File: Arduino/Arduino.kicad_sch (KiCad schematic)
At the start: 21 parts, among them J1 Conn_01x01, J10 Conn_01x03, J2 Conn_01x01, J3 Digital, J4 Digital, J5 ICSP, J6 Digital, J7 Digital, J8 Barrel_Jack_Switch, J9 Vcc, SW1 Reset, U1 ATmega328P-P, Y1 16MHz

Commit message: Some changes in arduino board.
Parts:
- added C1: 100n, symbol Device:C_Small
- added Q1, Q2: SS8050, Package_TO_SOT_SMD:SOT-23, symbol Transistor_BJT:SS8050
- added R1: 10k, symbol Device:R_Small
- renumbered C1 to C2, C2 to C3, C3 to C4, C4 to C5, C5 to C6, C6 to C7, J8 to J1, J7 to J10, J9 to J2, J10 to J3, J1 to J4, J2 to J5, J3 to J6, J4 to J7, J5 to J8, J6 to J9, R1 to R2, R2 to R3
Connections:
- net +5V: now also Q1.3 (C), Q2.3 (C)
- net GND: now also R1.1
- net RX: now also Q1.2 (E), Q2.2 (E), R1.2; no longer J10.1 (Pin_1)
- net Reset: now also C1.2
- new net CH340/DTR: C1.1
- new net RX1: Q1.1 (B)
- new net RX2: J10.1 (Pin_1), Q2.1 (B)
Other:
- added sheet CH340 (../ModuloCH340/ModuloCH340.kicad_sch)
- added sheet Reles (reles.kicad_sch)
- title: (none) -> My Custom Arduino

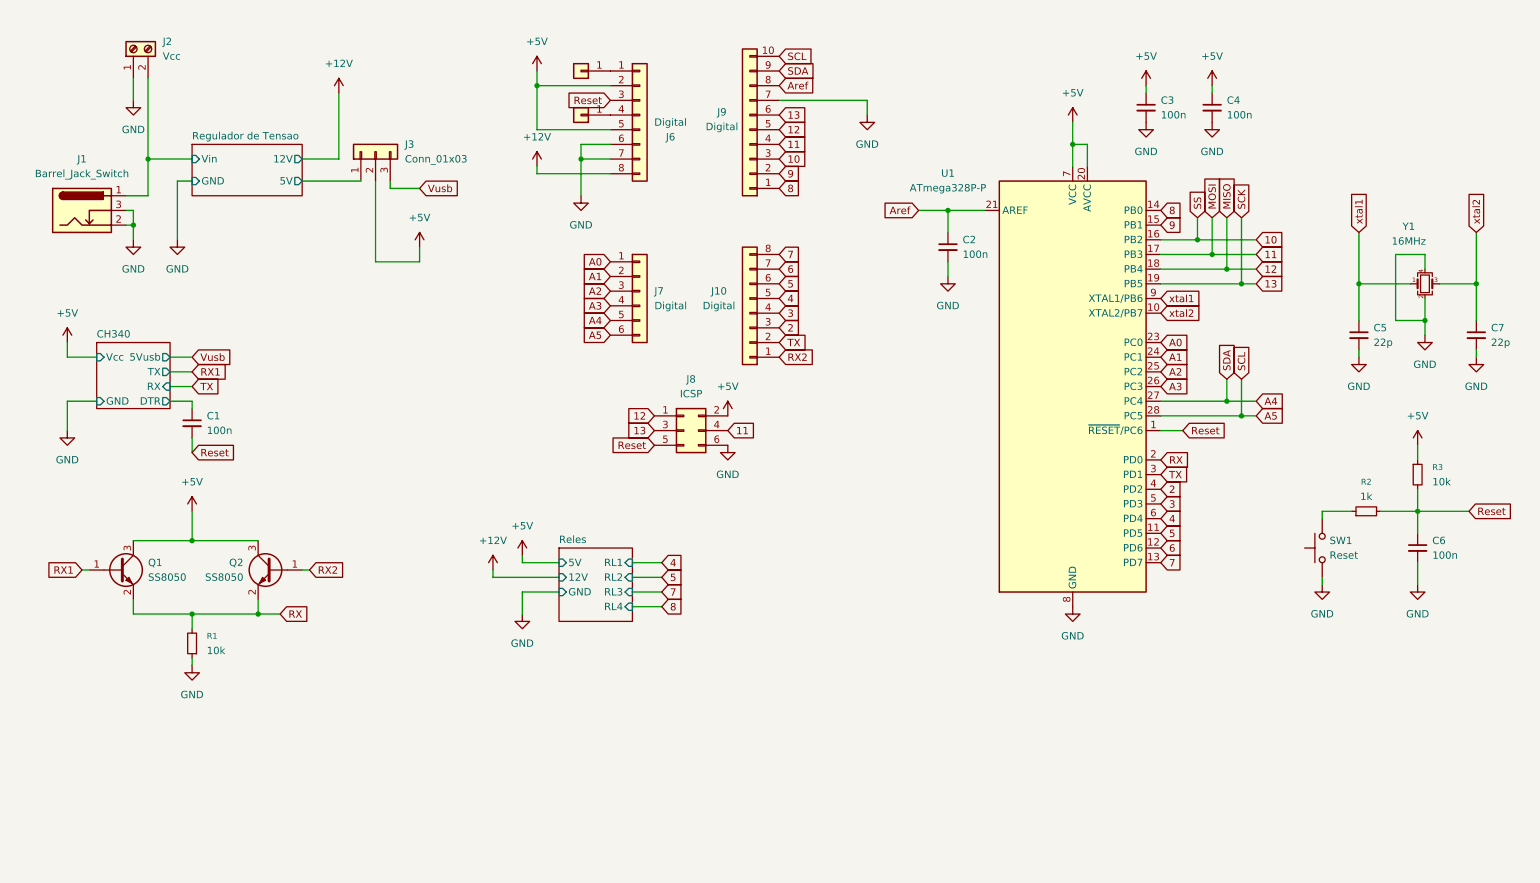
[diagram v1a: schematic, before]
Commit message: Completed circuit.
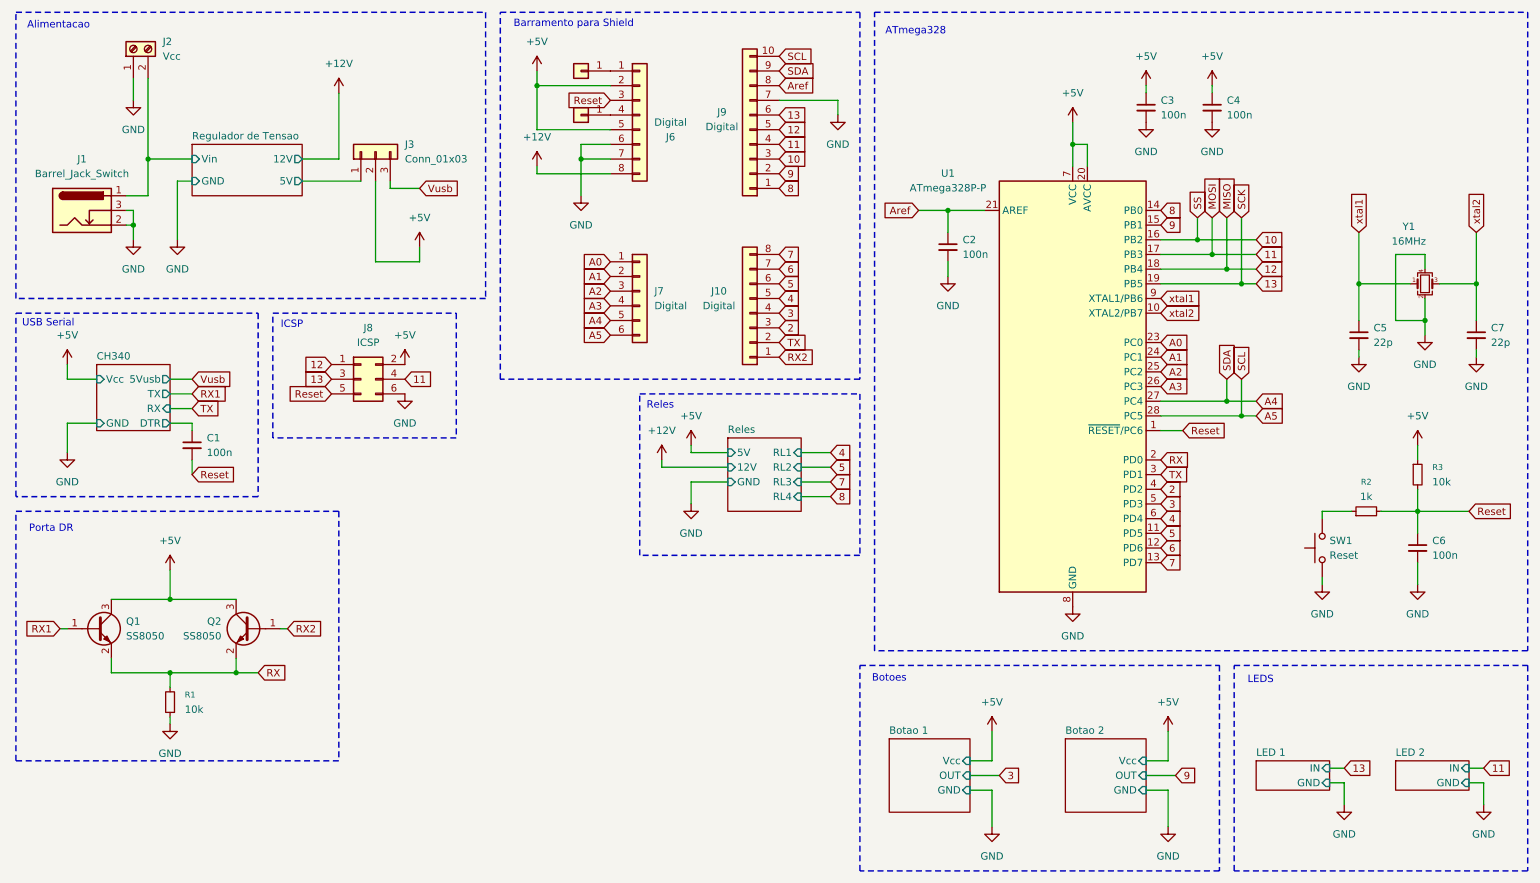
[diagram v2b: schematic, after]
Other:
- added sheet Botao 1 (/opt/repository/boards/ModuloBotao/ModuloBotao.kicad_sch)
- added sheet Botao 2 (/opt/repository/boards/ModuloBotao/ModuloBotao.kicad_sch)
- added sheet LED 1 (/opt/repository/boards/ModuloLED/ModuloLED.kicad_sch)
- added sheet LED 2 (/opt/repository/boards/ModuloLED/ModuloLED.kicad_sch)
- note added: "ATmega328"
- note added: "Alimentacao"
- note added: "Barramento para Shield"
- note added: "Botoes"
- note added: "ICSP"
- note added: "LEDS"
- note added: "Porta DR"
- note added: "Reles"
- note added: "USB Serial"
- moved on the sheet: C1, J8, Q1, Q2, R1

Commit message: Added all components to arduino pcb.
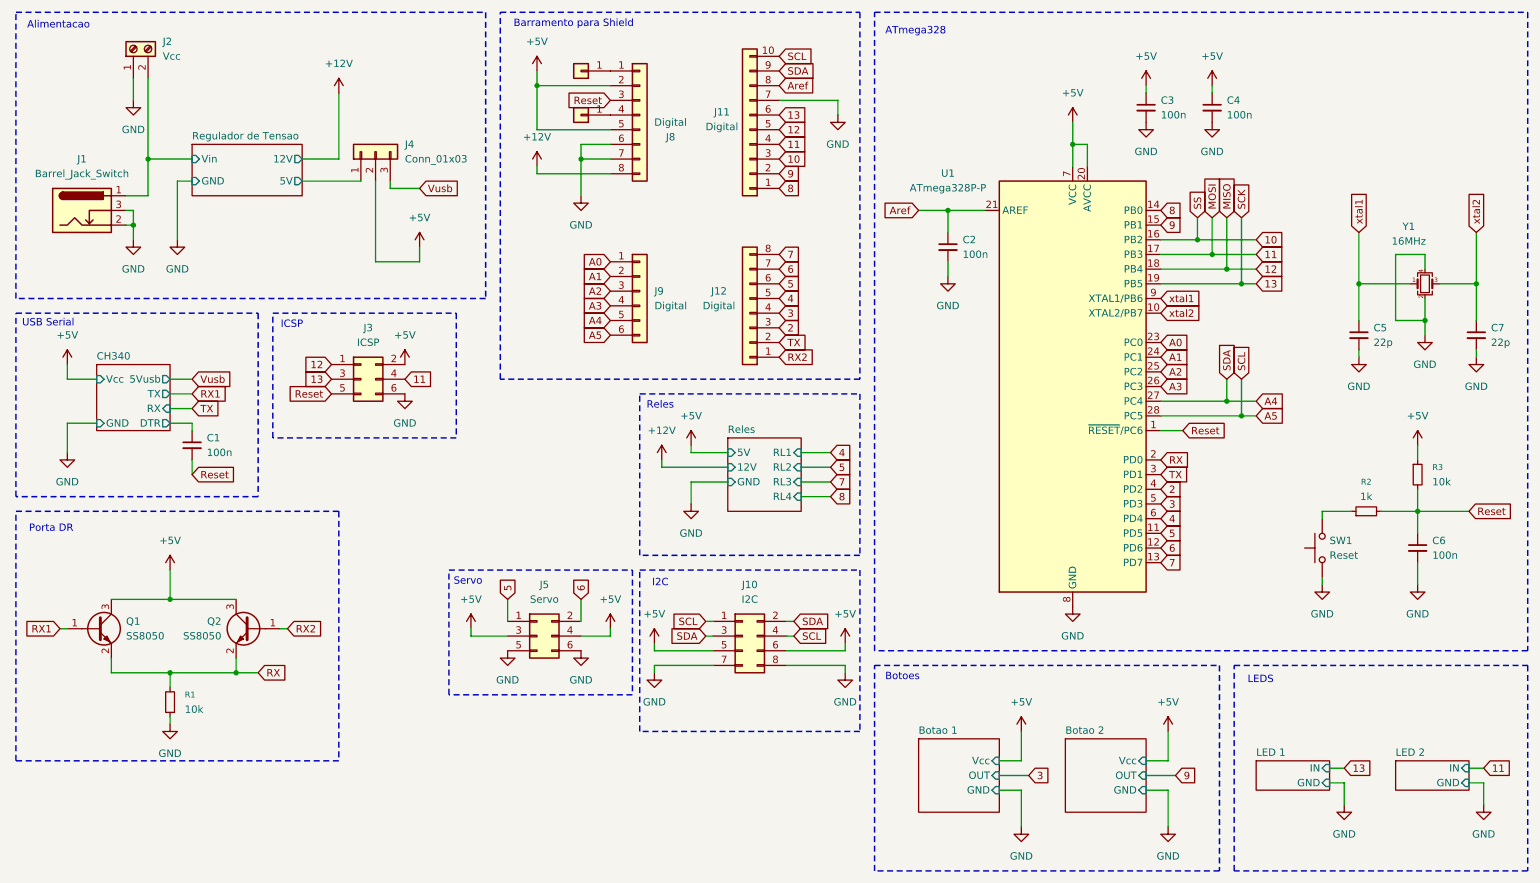
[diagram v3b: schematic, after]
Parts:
- added J10: I2C, Connector_PinHeader_2.54mm:PinHeader_2x04_P2.54mm_Vertical, symbol Connector_Generic:Conn_02x04_Odd_Even
- added J5: Servo, Connector_PinHeader_2.54mm:PinHeader_2x03_P2.54mm_Vertical, symbol Connector_Generic:Conn_02x03_Odd_Even
- C1, C2, C3, C4, C5, C6, C7: footprint (none) -> Capacitor_SMD:C_0805_2012Metric_Pad1.18x1.45mm_HandSolder
- J12: renamed from J10; footprint (none) -> Connector_PinHeader_2.54mm:PinHeader_1x08_P2.54mm_Vertical
- J6: renamed from J4; footprint (none) -> Connector_PinHeader_2.54mm:PinHeader_1x01_P2.54mm_Vertical
- J7: renamed from J5; footprint (none) -> Connector_PinHeader_2.54mm:PinHeader_1x01_P2.54mm_Vertical
- J8: renamed from J6; footprint (none) -> Connector_PinHeader_2.54mm:PinHeader_1x08_P2.54mm_Vertical
- J9: renamed from J7; footprint (none) -> Connector_PinHeader_2.54mm:PinHeader_1x06_P2.54mm_Vertical
- R1, R2, R3: footprint (none) -> Resistor_SMD:R_0805_2012Metric_Pad1.20x1.40mm_HandSolder
- SW1: footprint (none) -> Button_Switch_SMD:SW_SPST_TL3342
- renumbered J9 to J11, J8 to J3, J3 to J4
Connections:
- net +5V: now also J10.5 (Pin_5), J10.6 (Pin_6), J5.3 (Pin_3), J5.4 (Pin_4)
- net 5: now also J5.1 (Pin_1)
- net 6: now also J5.2 (Pin_2)
- net A4: now also J10.2 (Pin_2), J10.3 (Pin_3)
- net A5: now also J10.1 (Pin_1), J10.4 (Pin_4)
- net GND: now also J10.7 (Pin_7), J10.8 (Pin_8), J5.5 (Pin_5), J5.6 (Pin_6)
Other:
- note added: "I2C"
- note added: "Servo"

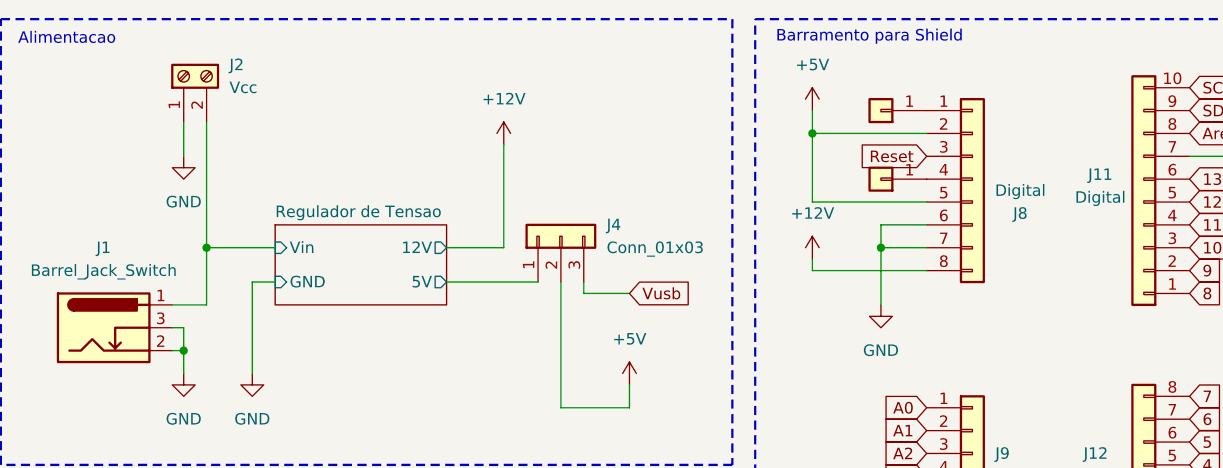
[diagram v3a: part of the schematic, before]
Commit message: Added all components to arduino pcb.
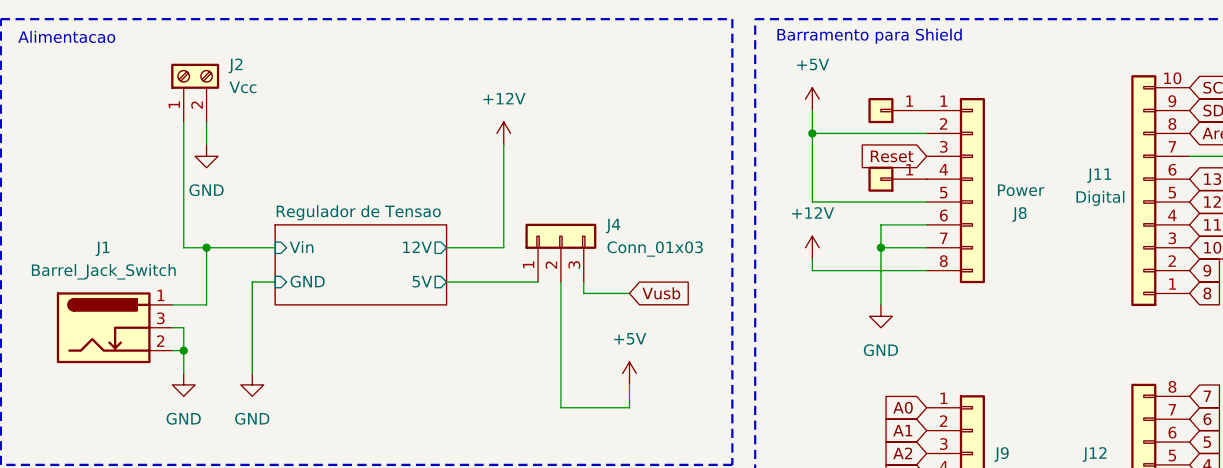
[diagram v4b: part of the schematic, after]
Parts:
- J8: value Digital -> Power
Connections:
- net GND: now also J2.2 (Pin_2); no longer J2.1 (Pin_1)
- net Regulador de Tensao/Vin: now also J2.1 (Pin_1); no longer J2.2 (Pin_2)
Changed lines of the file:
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@@
 	)
 	(junction
+		(at 36.83 39.37)
+		(diameter 0)
+		(color 0 0 0 0)
+	)
+	(junction
 		(at 34.29 50.8)
 		(diameter 0)
@@
 		(color 0 0 0 0)
 	)
-	(junction
-		(at 36.83 39.37)
-		(diameter 0)
-		(color 0 0 0 0)
-	)
 	(wire
 		(pts
@@
 	(wire
 		(pts
+			(xy 34.29 25.4) (xy 34.29 39.37)
+		)
+		(stroke
+			(width 0)
+			(type default)
+		)
+	)
+	(wire
+		(pts
 			(xy 134.62 127) (xy 124.46 127)
 		)
@@
 	(wire
 		(pts
-			(xy 209.55 148.59) (xy 213.36 148.59)
+			(xy 34.29 39.37) (xy 36.83 39.37)
 		)
 		(stroke
@@
 	(wire
 		(pts
-			(xy 63.5 43.18) (xy 73.66 43.18)
+			(xy 209.55 148.59) (xy 213.36 148.59)
 		)
 		(stroke
@@
 	(wire
 		(pts
-			(xy 22.86 85.09) (xy 22.86 90.17)
+			(xy 63.5 43.18) (xy 73.66 43.18)
 		)
 		(stroke
@@
 	(wire
 		(pts
-			(xy 34.29 25.4) (xy 34.29 29.21)
+			(xy 22.86 85.09) (xy 22.86 90.17)
 		)
 		(stroke
@@
 	(wire
 		(pts
-			(xy 36.83 25.4) (xy 36.83 39.37)
-		)
-		(stroke
-			(width 0)
-			(type default)
-		)
-	)
-	(wire
-		(pts
 			(xy 116.84 41.91) (xy 104.14 41.91)
 		)
@@
 	(wire
 		(pts
+			(xy 36.83 25.4) (xy 36.83 27.94)
+		)
+		(stroke
+			(width 0)
+			(type default)
+		)
+	)
+	(wire
+		(pts
 			(xy 149.86 97.79) (xy 154.94 97.79)
 		)
@@
 	(symbol
 		(lib_id "power:GND")
-		(at 34.29 29.21 0)
+		(at 36.83 27.94 0)
 		(unit 1)
 		(exclude_from_sim no)
@@
 		(fields_autoplaced yes)
 		(property "Reference" "#PWR03"
-			(at 34.29 35.56 0)
+			(at 36.83 34.29 0)
 			(effects
 				(font
@@
 		)
 		(property "Value" "GND"
-			(at 34.29 34.29 0)
+			(at 36.83 33.02 0)
 			(effects
 				(font
@@
 		)
 		(property "Footprint" ""
-			(at 34.29 29.21 0)
+			(at 36.83 27.94 0)
 			(effects
 				(font
@@
 		)
 		(property "Datasheet" ""
-			(at 34.29 29.21 0)
+			(at 36.83 27.94 0)
 			(effects
 				(font
@@
 		)
 		(property "Description" "Power symbol creates a global label with name \"GND\" , ground"
-			(at 34.29 29.21 0)
+			(at 36.83 27.94 0)
 			(effects
 				(font
@@
 	)
 	(symbol
-		(lib_id "Switch:SW_MEC_5G")
-		(at 240.03 106.68 90)
-		(unit 1)
-		(exclude_from_sim no)
-		(in_bom yes)
-		(on_board yes)
-		(dnp no)
-		(fields_autoplaced yes)
-		(property "Reference" "SW1"
-			(at 241.3 105.4099 90)
-			(effects
-				(font
-					(size 1.27 1.27)
-				)
-				(justify right)
-			)
-		)
-		(property "Value" "Reset"
-			(at 241.3 107.9499 90)
-			(effects
-				(font
-					(size 1.27 1.27)
-				)
-				(justify right)
-			)
-		)
-		(property "Footprint" "Button_Switch_SMD:SW_SPST_TL3342"
-			(at 234.95 106.68 0)
-			(effects
-				(font
-					(size 1.27 1.27)
-				)
-				(hide yes)
-			)
-		)
-		(property "Datasheet" "http://www.apem.com/int/index.php?controller=attachment&id_attachment=488"
-			(at 234.95 106.68 0)
-			(effects
-				(font
-					(size 1.27 1.27)
-				)
-				(hide yes)
-			)
-		)
-		(property "Description" "MEC 5G single pole normally-open tactile switch"
-			(at 240.03 106.68 0)
-			(effects
-				(font
-					(size 1.27 1.27)
-				)
-				(hide yes)
-			)
-		)
-		(pin "3"
-		)
-		(pin "2"
-		)
-		(pin "4"
-		)
-		(pin "1"
-		)
-		(instances
-			(project ""
-				(path "/b1260de1-9c48-4b08-a759-f31e40d6183e"
-					(reference "SW1")
-					(unit 1)
-				)
-			)
-		)
-	)
-	(symbol
 		(lib_id "power:GND")
 		(at 246.38 73.66 0)
@@
 	)
 	(symbol
+		(lib_id "Switch:SW_MEC_5G")
+		(at 240.03 106.68 90)
+		(unit 1)
+		(exclude_from_sim no)
+		(in_bom yes)
+		(on_board yes)
+		(dnp no)
+		(fields_autoplaced yes)
+		(property "Reference" "SW1"
+			(at 241.3 105.4099 90)
+			(effects
+				(font
+					(size 1.27 1.27)
+				)
+				(justify right)
+			)
+		)
+		(property "Value" "Reset"
+			(at 241.3 107.9499 90)
+			(effects
+				(font
+					(size 1.27 1.27)
+				)
+				(justify right)
+			)
+		)
+		(property "Footprint" "Button_Switch_SMD:SW_SPST_TL3342"
+			(at 234.95 106.68 0)
+			(effects
+				(font
+					(size 1.27 1.27)
+				)
+				(hide yes)
+			)
+		)
+		(property "Datasheet" "http://www.apem.com/int/index.php?controller=attachment&id_attachment=488"
+			(at 234.95 106.68 0)
+			(effects
+				(font
+					(size 1.27 1.27)
+				)
+				(hide yes)
+			)
+		)
+		(property "Description" "MEC 5G single pole normally-open tactile switch"
+			(at 240.03 106.68 0)
+			(effects
+				(font
+					(size 1.27 1.27)
+				)
+				(hide yes)
+			)
+		)
+		(pin "3"
+		)
+		(pin "2"
+		)
+		(pin "4"
+		)
+		(pin "1"
+		)
+		(instances
+			(project "Arduino"
+				(path "/b1260de1-9c48-4b08-a759-f31e40d6183e"
+					(reference "SW1")
+					(unit 1)
+				)
+			)
+		)
+	)
+	(symbol
 		(lib_id "power:GND")
 		(at 22.86 90.17 0)
@@
 			)
 		)
-		(property "Value" "Digital"
+		(property "Value" "Power"
 			(at 127.254 33.02 0)
 			(effects

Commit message: First version from PCB schematic.
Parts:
- added JP1: A, Jumper:SolderJumper-2_P1.3mm_Bridged2Bar_RoundedPad1.0x1.5mm, symbol Jumper:SolderJumper_2_Bridged
- added RV1: 100k, Potentiometer_THT:Potentiometer_Bourns_3296W_Vertical, symbol Device:R_Potentiometer_Trim
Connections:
- net +5V: now also RV1.1
- net 5: now also J5.2 (Pin_2); no longer J5.1 (Pin_1)
- net 6: now also J5.1 (Pin_1); no longer J5.2 (Pin_2)
- net A0: now also JP1.2 (B)
- net GND: now also RV1.3
- net Regulador de Tensao/5V renamed Regulador de Tensao/+5V
- new net: JP1.1 (A), RV1.2
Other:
- sheet Regulador de Tensao ports: added +12V, +5V; removed 12V, 5V
- sheet Reles ports: added +12V, +5V; removed 12V, 5V
- note added: "Trimpot"
